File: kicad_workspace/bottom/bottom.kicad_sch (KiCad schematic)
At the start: 1 part, among them M1 N20_MOTOR_EXTENDED_SHAFT

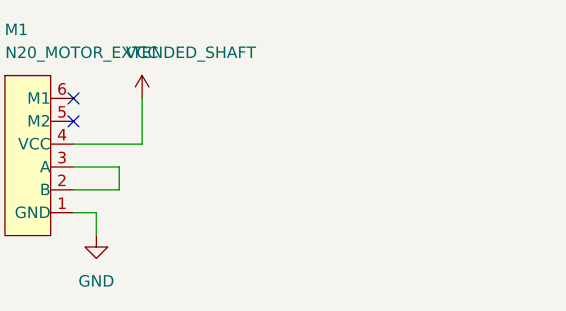
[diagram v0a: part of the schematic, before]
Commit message: changed pcb shape dimensions. imported shape into pcb
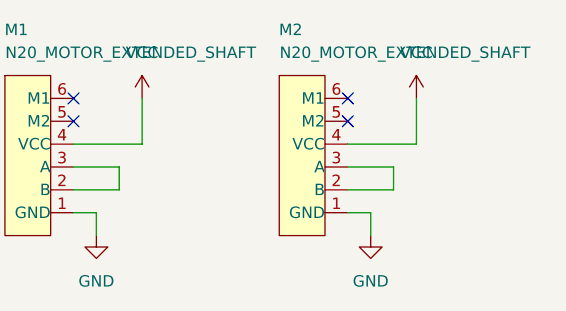
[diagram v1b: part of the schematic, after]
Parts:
- added M2: N20_MOTOR_EXTENDED_SHAFT, pololu:N20_EXTENDED_SHAFT, symbol pololu:N20_MOTOR_EXTENDED_SHAFT
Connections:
- net GND: now also M2.1 (GND)
- net VCC: now also M2.4 (VCC)
- new net: M2.2 (B), M2.3 (A)
- no-connect marks 2 -> 4
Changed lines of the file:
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@@
-(kicad_sch (version 20211123) (generator eeschema)
+(kicad_sch (version 20230121) (generator eeschema)
   (paper "A4")
   (no_connect (at 40.64 43.18))
+  (no_connect (at 71.12 45.72))
   (no_connect (at 40.64 45.72))
+  (no_connect (at 71.12 43.18))
   (wire (pts (xy 40.64 55.88) (xy 43.18 55.88))
-    (stroke (width 0) (type default) (color 0 0 0 0))
+    (stroke (width 0) (type default))
+  )
+  (wire (pts (xy 73.66 58.42) (xy 73.66 55.88))
+    (stroke (width 0) (type default))
   )
   (wire (pts (xy 45.72 53.34) (xy 45.72 50.8))
-    (stroke (width 0) (type default) (color 0 0 0 0))
+    (stroke (width 0) (type default))
+  )
+  (wire (pts (xy 71.12 48.26) (xy 78.74 48.26))
+    (stroke (width 0) (type default))
+  )
+  (wire (pts (xy 71.12 55.88) (xy 73.66 55.88))
+    (stroke (width 0) (type default))
+  )
+  (wire (pts (xy 71.12 53.34) (xy 76.2 53.34))
+    (stroke (width 0) (type default))
   )
   (wire (pts (xy 48.26 48.26) (xy 48.26 43.18))
-    (stroke (width 0) (type default) (color 0 0 0 0))
+    (stroke (width 0) (type default))
   )
   (wire (pts (xy 43.18 58.42) (xy 43.18 55.88))
-    (stroke (width 0) (type default) (color 0 0 0 0))
+    (stroke (width 0) (type default))
   )
   (wire (pts (xy 40.64 53.34) (xy 45.72 53.34))
-    (stroke (width 0) (type default) (color 0 0 0 0))
+    (stroke (width 0) (type default))
   )
   (wire (pts (xy 40.64 50.8) (xy 45.72 50.8))
-    (stroke (width 0) (type default) (color 0 0 0 0))
+    (stroke (width 0) (type default))
   )
   (wire (pts (xy 40.64 48.26) (xy 48.26 48.26))
-    (stroke (width 0) (type default) (color 0 0 0 0))
+    (stroke (width 0) (type default))
+  )
+  (wire (pts (xy 71.12 50.8) (xy 76.2 50.8))
+    (stroke (width 0) (type default))
+  )
+  (wire (pts (xy 76.2 53.34) (xy 76.2 50.8))
+    (stroke (width 0) (type default))
+  )
+  (wire (pts (xy 78.74 48.26) (xy 78.74 43.18))
+    (stroke (width 0) (type default))
+  )
+  (symbol (lib_id "power:GND") (at 73.66 58.42 0) (unit 1)
+    (in_bom yes) (on_board yes) (dnp no) (fields_autoplaced)
+    (property "Reference" "#PWR01" (at 73.66 64.77 0)
+      (effects (font (size 1.27 1.27)) hide)
+    )
+    (property "Value" "GND" (at 73.66 63.5 0)
+      (effects (font (size 1.27 1.27)))
+    )
+    (property "Footprint" "" (at 73.66 58.42 0)
+      (effects (font (size 1.27 1.27)) hide)
+    )
+    (property "Datasheet" "" (at 73.66 58.42 0)
+      (effects (font (size 1.27 1.27)) hide)
+    )
+    (pin "1")
+    (instances
+      (project "bottom"
+        (path "/8949e4cc-98fb-401d-bf78-7a26c685fd98"
+          (reference "#PWR01") (unit 1)
+        )
+      )
+    )
   )
   (symbol (lib_id "power:VCC") (at 48.26 43.18 0) (unit 1)
-    (in_bom yes) (on_board yes) (fields_autoplaced)
-    (property "Reference" "#PWR?" (id 0) (at 48.26 46.99 0)
-      (effects (font (size 1.27 1.27)) hide)
-    )
-    (property "Value" "VCC" (id 1) (at 48.26 38.1 0))
-    (property "Footprint" "" (id 2) (at 48.26 43.18 0)
-      (effects (font (size 1.27 1.27)) hide)
-    )
-    (property "Datasheet" "" (id 3) (at 48.26 43.18 0)
-      (effects (font (size 1.27 1.27)) hide)
-    )
-    (pin "1")
+    (in_bom yes) (on_board yes) (dnp no) (fields_autoplaced)
+    (property "Reference" "#PWR?" (at 48.26 46.99 0)
+      (effects (font (size 1.27 1.27)) hide)
+    )
+    (property "Value" "VCC" (at 48.26 38.1 0)
+      (effects (font (size 1.27 1.27)))
+    )
+    (property "Footprint" "" (at 48.26 43.18 0)
+      (effects (font (size 1.27 1.27)) hide)
+    )
+    (property "Datasheet" "" (at 48.26 43.18 0)
+      (effects (font (size 1.27 1.27)) hide)
+    )
+    (pin "1")
+    (instances
+      (project "bottom"
+        (path "/8949e4cc-98fb-401d-bf78-7a26c685fd98"
+          (reference "#PWR?") (unit 1)
+        )
+      )
+    )
+  )
+  (symbol (lib_id "power:VCC") (at 78.74 43.18 0) (unit 1)
+    (in_bom yes) (on_board yes) (dnp no) (fields_autoplaced)
+    (property "Reference" "#PWR02" (at 78.74 46.99 0)
+      (effects (font (size 1.27 1.27)) hide)
+    )
+    (property "Value" "VCC" (at 78.74 38.1 0)
+      (effects (font (size 1.27 1.27)))
+    )
+    (property "Footprint" "" (at 78.74 43.18 0)
+      (effects (font (size 1.27 1.27)) hide)
+    )
+    (property "Datasheet" "" (at 78.74 43.18 0)
+      (effects (font (size 1.27 1.27)) hide)
+    )
+    (pin "1")
+    (instances
+      (project "bottom"
+        (path "/8949e4cc-98fb-401d-bf78-7a26c685fd98"
+          (reference "#PWR02") (unit 1)
+        )
+      )
+    )
   )
   (symbol (lib_id "power:GND") (at 43.18 58.42 0) (unit 1)
-    (in_bom yes) (on_board yes) (fields_autoplaced)
-    (property "Reference" "#PWR?" (id 0) (at 43.18 64.77 0)
-      (effects (font (size 1.27 1.27)) hide)
-    )
-    (property "Value" "GND" (id 1) (at 43.18 63.5 0))
-    (property "Footprint" "" (id 2) (at 43.18 58.42 0)
-      (effects (font (size 1.27 1.27)) hide)
-    )
-    (property "Datasheet" "" (id 3) (at 43.18 58.42 0)
-      (effects (font (size 1.27 1.27)) hide)
-    )
-    (pin "1")
-  )
-  (symbol (lib_id "pololu:N20_MOTOR_EXTENDED_SHAFT") (at 33.02 40.64 0) (unit 1)
-    (in_bom yes) (on_board yes)
-    (property "Reference" "M1" (id 0) (at 34.29 35.56 0))
-    (property "Value" "N20_MOTOR_EXTENDED_SHAFT" (id 1) (at 46.99 38.1 0))
-    (property "Footprint" "pololu:N20_EXTENDED_SHAFT" (id 2) (at 46.355 37.465 0)
-      (effects (font (size 1.27 1.27)) hide)
-    )
-    (property "Datasheet" "" (id 3) (at 34.925 40.64 0)
+    (in_bom yes) (on_board yes) (dnp no) (fields_autoplaced)
+    (property "Reference" "#PWR?" (at 43.18 64.77 0)
+      (effects (font (size 1.27 1.27)) hide)
+    )
+    (property "Value" "GND" (at 43.18 63.5 0)
+      (effects (font (size 1.27 1.27)))
+    )
+    (property "Footprint" "" (at 43.18 58.42 0)
+      (effects (font (size 1.27 1.27)) hide)
+    )
+    (property "Datasheet" "" (at 43.18 58.42 0)
+      (effects (font (size 1.27 1.27)) hide)
+    )
+    (pin "1")
+    (instances
+      (project "bottom"
+        (path "/8949e4cc-98fb-401d-bf78-7a26c685fd98"
+          (reference "#PWR?") (unit 1)
+        )
+      )
+    )
+  )
+  (symbol (lib_id "pololu:N20_MOTOR_EXTENDED_SHAFT") (at 63.5 40.64 0) (unit 1)
+    (in_bom yes) (on_board yes) (dnp no)
+    (property "Reference" "M2" (at 64.77 35.56 0)
+      (effects (font (size 1.27 1.27)))
+    )
+    (property "Value" "N20_MOTOR_EXTENDED_SHAFT" (at 77.47 38.1 0)
+      (effects (font (size 1.27 1.27)))
+    )
+    (property "Footprint" "pololu:N20_EXTENDED_SHAFT" (at 76.835 37.465 0)
+      (effects (font (size 1.27 1.27)) hide)
+    )
+    (property "Datasheet" "" (at 65.405 40.64 0)
       (effects (font (size 1.27 1.27)) hide)
     )
@@
     (pin "5")
     (pin "6")
+    (instances
+      (project "bottom"
+        (path "/8949e4cc-98fb-401d-bf78-7a26c685fd98"
+          (reference "M2") (unit 1)
+        )
+      )
+    )
+  )
+  (symbol (lib_id "pololu:N20_MOTOR_EXTENDED_SHAFT") (at 33.02 40.64 0) (unit 1)
+    (in_bom yes) (on_board yes) (dnp no)
+    (property "Reference" "M1" (at 34.29 35.56 0)
+      (effects (font (size 1.27 1.27)))
+    )
+    (property "Value" "N20_MOTOR_EXTENDED_SHAFT" (at 46.99 38.1 0)
+      (effects (font (size 1.27 1.27)))
+    )
+    (property "Footprint" "pololu:N20_EXTENDED_SHAFT" (at 46.355 37.465 0)
+      (effects (font (size 1.27 1.27)) hide)
+    )
+    (property "Datasheet" "" (at 34.925 40.64 0)
+      (effects (font (size 1.27 1.27)) hide)
+    )
+    (pin "1")
+    (pin "2")
+    (pin "3")
+    (pin "4")
+    (pin "5")
+    (pin "6")
+    (instances
+      (project "bottom"
+        (path "/8949e4cc-98fb-401d-bf78-7a26c685fd98"
+          (reference "M1") (unit 1)
+        )
+      )
+    )
   )
   (sheet_instances
     (path "/" (page "1"))
   )
-  (symbol_instances
-    (path "/b8430d9e-730b-49b7-8095-ed84876da861"
-      (reference "#PWR?") (unit 1) (value "VCC") (footprint "")
-    )
-    (path "/ce09e886-c93f-4674-9961-575863530056"
-      (reference "#PWR?") (unit 1) (value "GND") (footprint "")
-    )
-    (path "/f1b9d147-fb95-45c1-a371-9168d76297c0"
-      (reference "M1") (unit 1) (value "N20_MOTOR_EXTENDED_SHAFT") (footprint "pololu:N20_EXTENDED_SHAFT")
-    )
-  )
 )

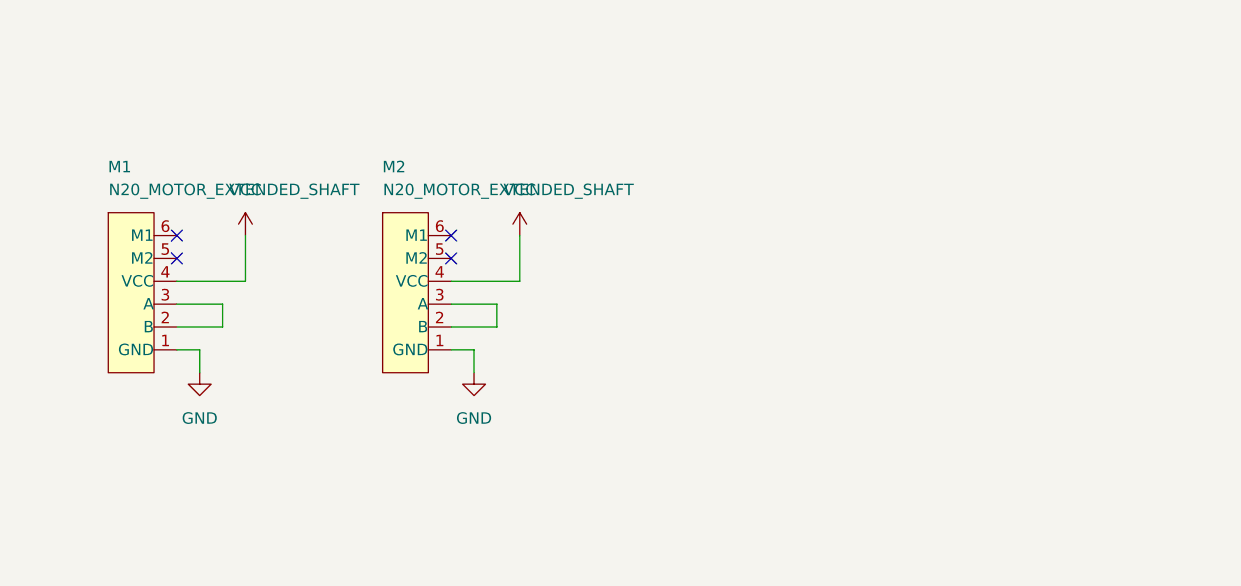
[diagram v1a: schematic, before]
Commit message: add drv8833 - motor driver
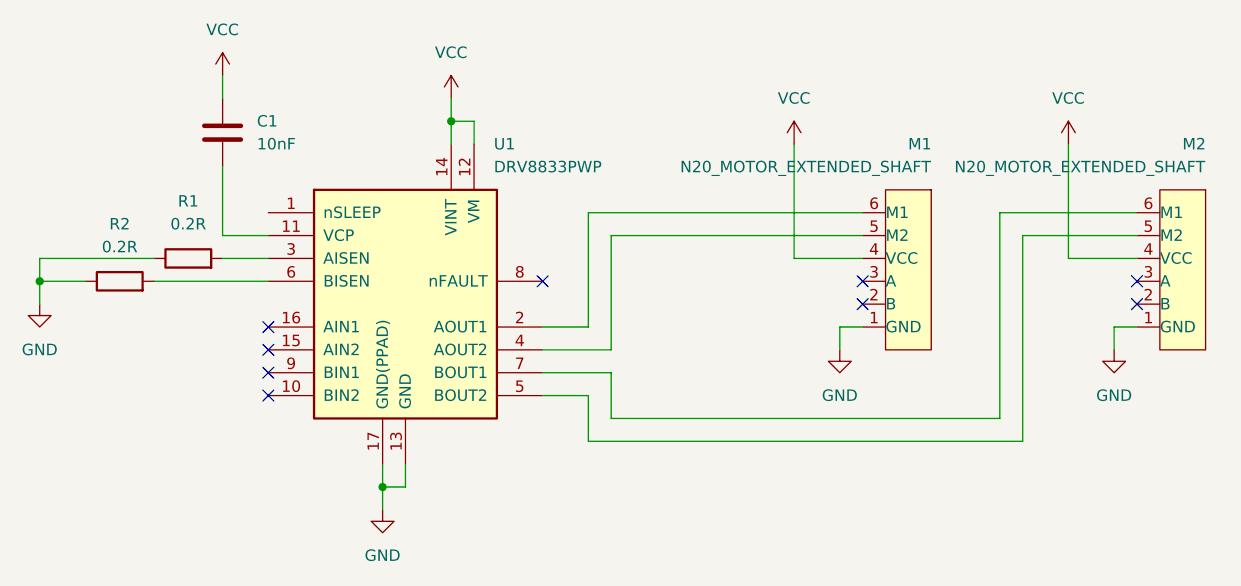
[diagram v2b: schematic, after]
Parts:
- added C1: 10nF, symbol Device:C
- added R1, R2: 0.2R, symbol Device:R
- added U1: DRV8833PWP, Package_SO:HTSSOP-16-1EP_4.4x5mm_P0.65mm_EP3.4x5mm_Mask2.46x2.31mm_ThermalVias, symbol Driver_Motor:DRV8833PWP
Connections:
- net GND: now also R1.1, R2.1, U1.13 (GND), U1.17 (GND(PPAD))
- net VCC: now also C1.1, U1.12 (VM), U1.14 (VINT)
- net at M2.2 (B): no longer M2.3 (A)
- net at M2.5 (M2): now also U1.5 (BOUT2)
- net at M2.6 (M1): now also U1.7 (BOUT1)
- net at M1.2 (B): no longer M1.3 (A)
- net at M1.5 (M2): now also U1.4 (AOUT2)
- net at M1.6 (M1): now also U1.2 (AOUT1)
- new net: C1.2, U1.11 (VCP)
- new net: R1.2, U1.3 (AISEN)
- new net: R2.2, U1.6 (BISEN)
- no-connect marks 4 -> 9
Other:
- moved on the sheet: M1, M2

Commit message: add ultrasound model, footprint and symbol. add motor driver to schematic for learning kicad
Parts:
- added U2: ULTRASOUND_T_R, pololu:ULTRASOUND_T_R, symbol pololu:ULTRASOUND_T_R
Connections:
- net GND: now also U2.1 (GND)
- net at R2.2, U1.6 (BISEN): now also U2.2 (SIG)
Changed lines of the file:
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@@
   (junction (at 63.5 71.12) (diameter 0) (color 0 0 0 0)
+  )
+  (junction (at 48.26 48.26) (diameter 0) (color 0 0 0 0)
   )
   (junction (at 25.4 48.26) (diameter 0) (color 0 0 0 0)
@@
     (stroke (width 0) (type default))
   )
+  (wire (pts (xy 40.64 68.58) (xy 48.26 68.58))
+    (stroke (width 0) (type default))
+  )
   (wire (pts (xy 86.36 60.96) (xy 86.36 66.04))
     (stroke (width 0) (type default))
   )
+  (wire (pts (xy 40.64 71.12) (xy 63.5 71.12))
+    (stroke (width 0) (type default))
+  )
   (wire (pts (xy 63.5 71.12) (xy 63.5 73.66))
     (stroke (width 0) (type default))
@@
     (stroke (width 0) (type default))
   )
+  (wire (pts (xy 48.26 48.26) (xy 50.8 48.26))
+    (stroke (width 0) (type default))
+  )
   (wire (pts (xy 114.3 55.88) (xy 114.3 53.34))
     (stroke (width 0) (type default))
@@
     (stroke (width 0) (type default))
   )
-  (wire (pts (xy 38.1 48.26) (xy 50.8 48.26))
+  (wire (pts (xy 38.1 48.26) (xy 48.26 48.26))
     (stroke (width 0) (type default))
   )
@@
   )
   (wire (pts (xy 86.36 40.64) (xy 86.36 53.34))
+    (stroke (width 0) (type default))
+  )
+  (wire (pts (xy 48.26 68.58) (xy 48.26 48.26))
     (stroke (width 0) (type default))
   )
@@
         )
       )
+    )
+  )
+  (symbol (lib_id "pololu:ULTRASOUND_T_R") (at 40.64 73.66 180) (unit 1)
+    (in_bom yes) (on_board yes) (dnp no) (fields_autoplaced)
+    (property "Reference" "U2" (at 35.56 60.96 0)
+      (effects (font (size 1.27 1.27)))
+    )
+    (property "Value" "ULTRASOUND_T_R" (at 35.56 63.5 0)
+      (effects (font (size 1.27 1.27)))
+    )
+    (property "Footprint" "pololu:ULTRASOUND_T_R" (at 40.64 73.66 0)
+      (effects (font (size 1.27 1.27)) hide)
+    )
+    (property "Datasheet" "" (at 40.64 73.66 0)
+      (effects (font (size 1.27 1.27)) hide)
+    )
+    (pin "1")
+    (pin "2")
+    (instances
+      (project "bottom"
+        (path "/8949e4cc-98fb-401d-bf78-7a26c685fd98"
+          (reference "U2") (unit 1)
+        )
+      )

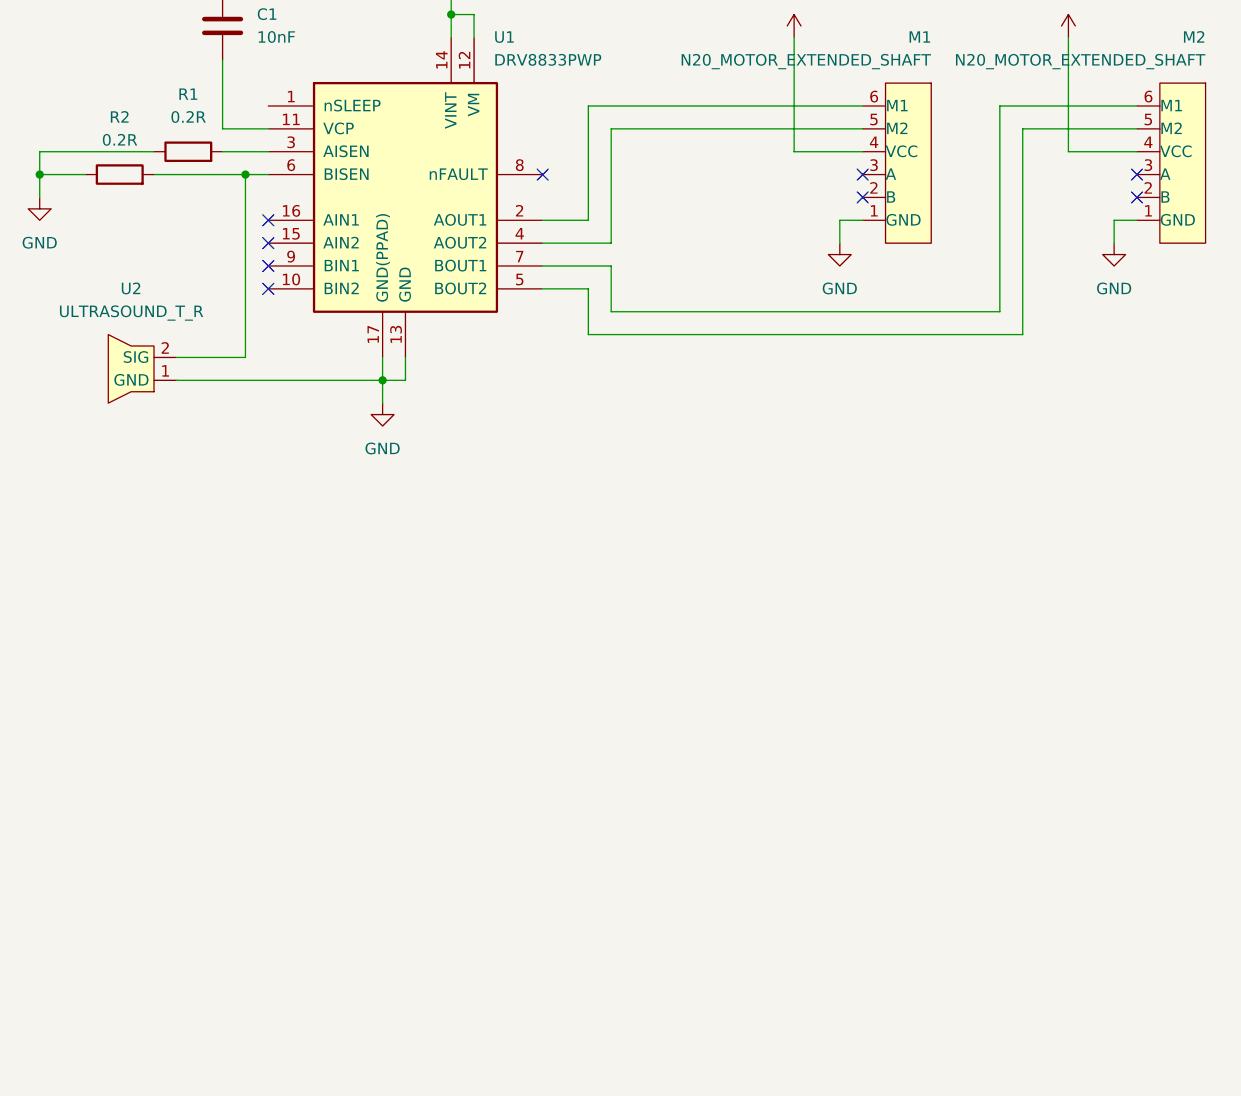
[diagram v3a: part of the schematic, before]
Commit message: add example stm32 uC, add simple footprint for step-up board
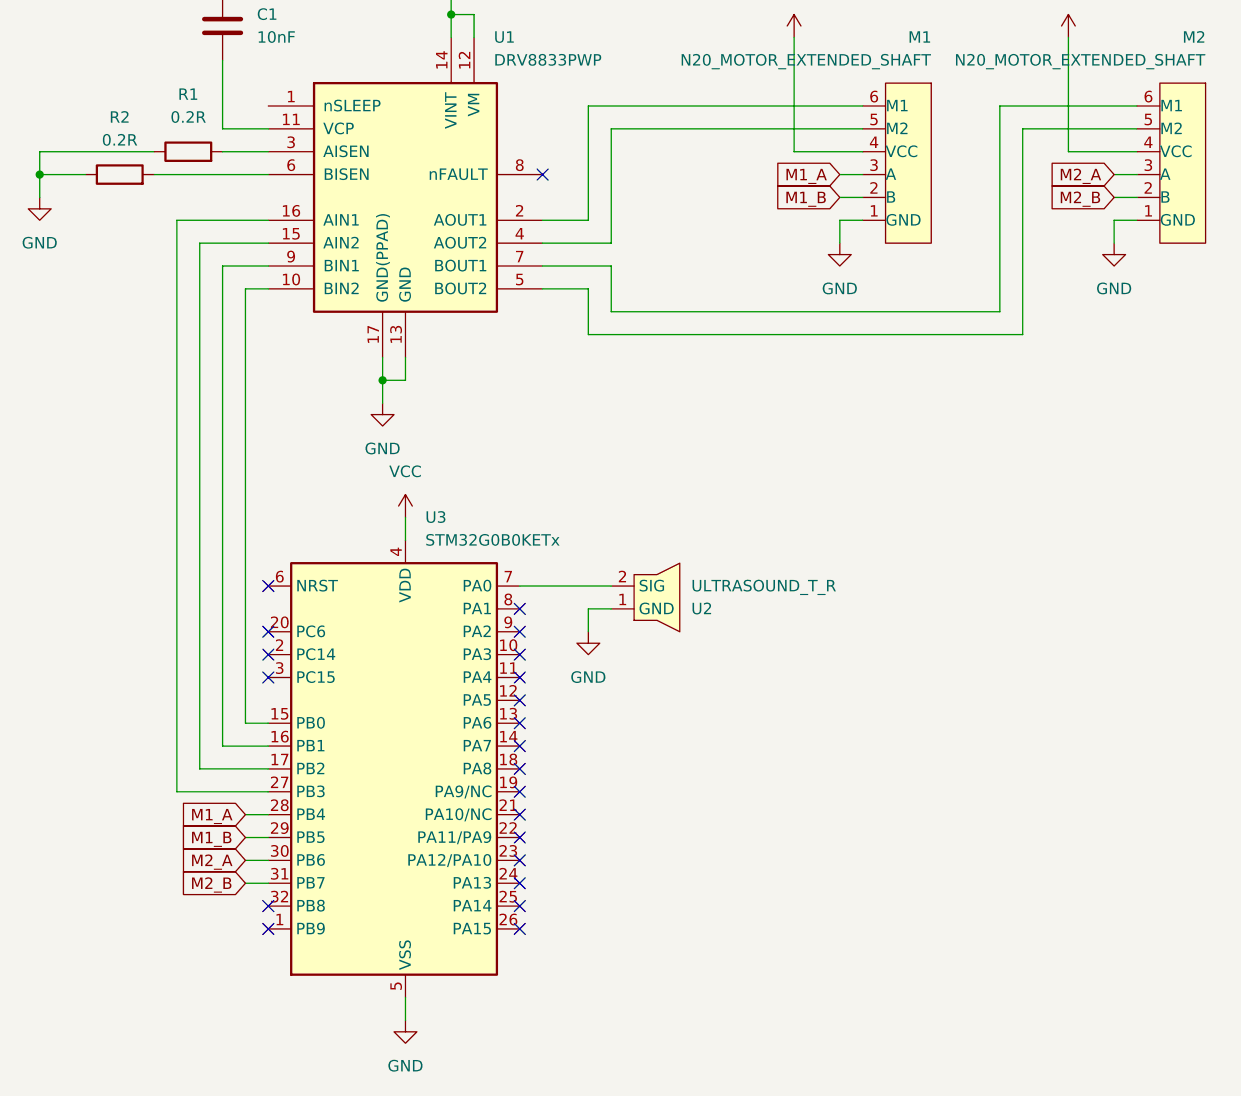
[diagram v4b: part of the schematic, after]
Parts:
- added U3: STM32G0B0KETx, Package_QFP:LQFP-32_7x7mm_P0.8mm, symbol MCU_ST_STM32G0:STM32G0B0KETx
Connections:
- net GND: now also U3.5 (VSS)
- net VCC: now also U3.4 (VDD)
- net at U1.10 (BIN2): now also U3.15 (PB0)
- net at U1.15 (AIN2): now also U3.17 (PB2)
- net at U1.16 (AIN1): now also U3.27 (PB3)
- net at R2.2, U1.6 (BISEN): no longer U2.2 (SIG)
- net at U1.9 (BIN1): now also U3.16 (PB1)
- net M2_B: now reaches M2.2 (B)
- net M2_B: now also U3.31 (PB7)
- net M2_A: now reaches M2.3 (A)
- net M2_A: now also U3.30 (PB6)
- net M1_B: now reaches M1.2 (B)
- net M1_B: now also U3.29 (PB5)
- net M1_A: now reaches M1.3 (A)
- net M1_A: now also U3.28 (PB4)
- new net: U2.2 (SIG), U3.7 (PA0)
- no-connect marks 9 -> 22
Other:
- moved on the sheet: U2

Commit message: small updates on parts
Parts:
- removed U3: STM32G0B0KETx, Package_QFP:LQFP-32_7x7mm_P0.8mm, symbol MCU_ST_STM32G0:STM32G0B0KETx
- added C2: 100nF, symbol Device:C
- added C3: 10uF, symbol Device:C_Polarized
- added R3: R, symbol Device:R
- added U3: ATmega4809-A, Package_QFP:TQFP-48_7x7mm_P0.5mm, symbol MCU_Microchip_ATmega:ATmega4809-A
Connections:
- net GND: now also C2.2, C3.2, U3.15 (GND), U3.29 (GND), U3.43 (GND)
- net M1_A: now also U3.44 (PA0)
- net M1_B: now also U3.45 (PA1)
- net M2_A: now also U3.46 (PA2)
- net M2_B: now also U3.47 (PA3)
- net VCC: now also C2.1, C3.1, U3.14 (VCC), U3.28 (AVCC), U3.42 (VCC)
- net at U1.10 (BIN2): now also U3.34 (PF0)
- net at U1.15 (AIN2): now also U3.36 (PF2)
- net at U1.16 (AIN1): now also U3.37 (PF3)
- net at U1.9 (BIN1): now also U3.35 (PF1)
- net at U2.2 (SIG): now also R3.2
- new net: R3.1, U3.48 (PA4)
- no-connect marks 22 -> 1
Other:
- moved on the sheet: U2
